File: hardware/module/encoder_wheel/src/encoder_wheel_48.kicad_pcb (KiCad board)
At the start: 2 copper layers, 74 x 74 mm, 2 parts

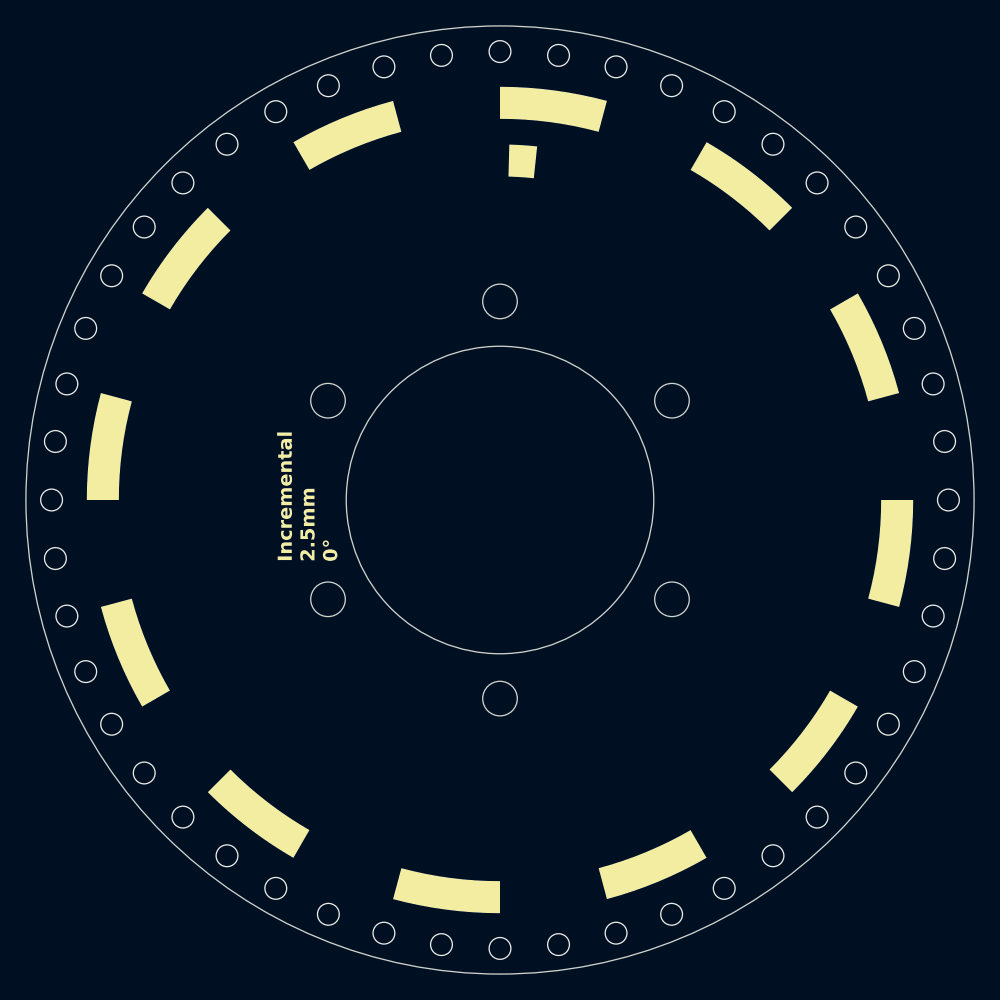
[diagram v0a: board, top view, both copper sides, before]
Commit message: Change sidepanel IR resistor to 15ohm and finalize encoder wheel design
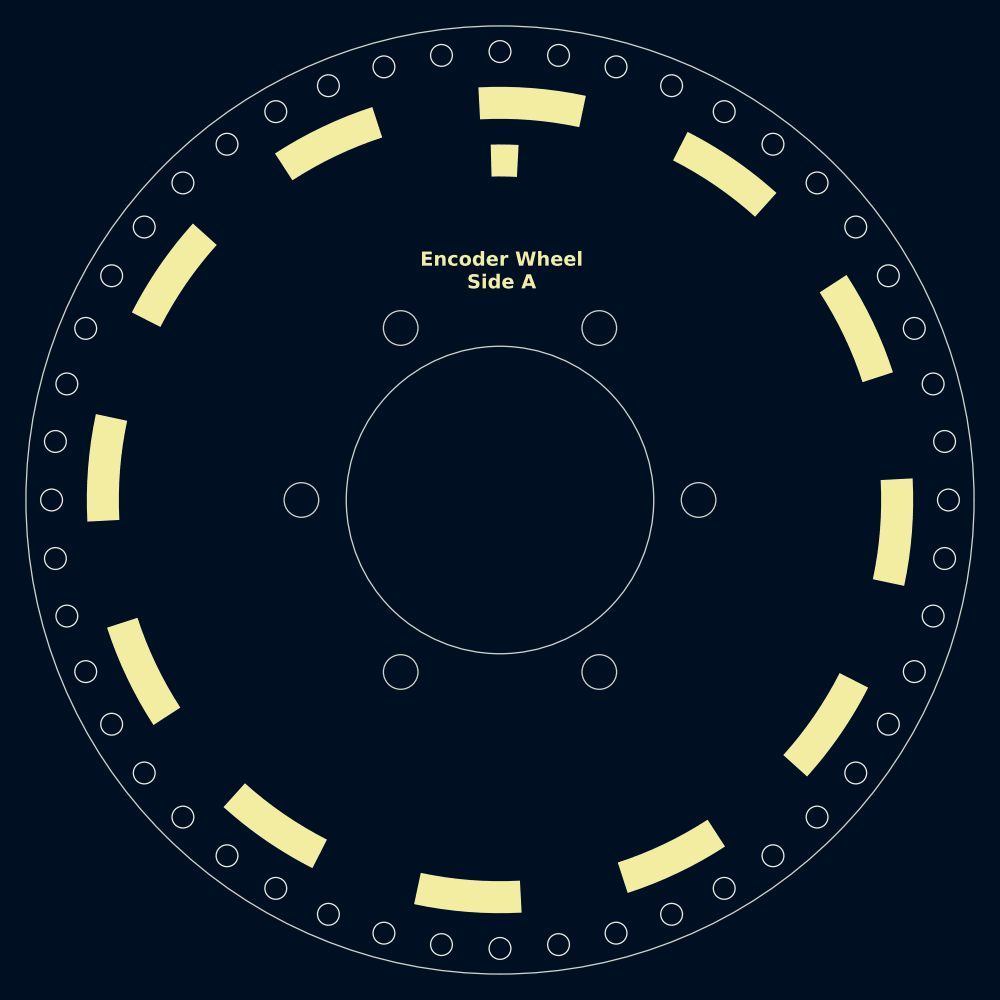
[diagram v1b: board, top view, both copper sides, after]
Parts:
- turned REF** to 3 degrees
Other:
- outline, holes or cut-outs redrawn
- board text added: "Encoder Wheel Side A"
- board text added: "Encoder Wheel Side B"
- board text removed: "Incremental 2.5mm 0°"
- board text removed: "Incremental 2.5mm 3.75°"
